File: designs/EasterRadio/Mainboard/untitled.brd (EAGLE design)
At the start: 236 x 57.5 mm, 51 parts, among them IC1 74HC595D, IC2 74HC595D, IC3 74HC595D, IC4 Analog Digital

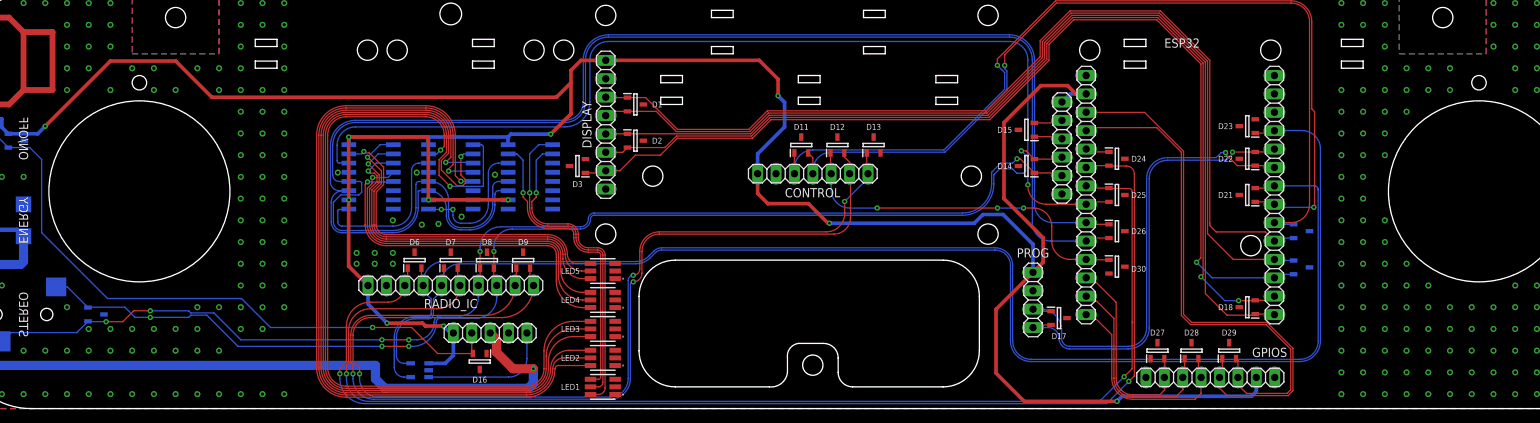
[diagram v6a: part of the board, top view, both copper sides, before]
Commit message: changes for new design excluding swap for amplifier
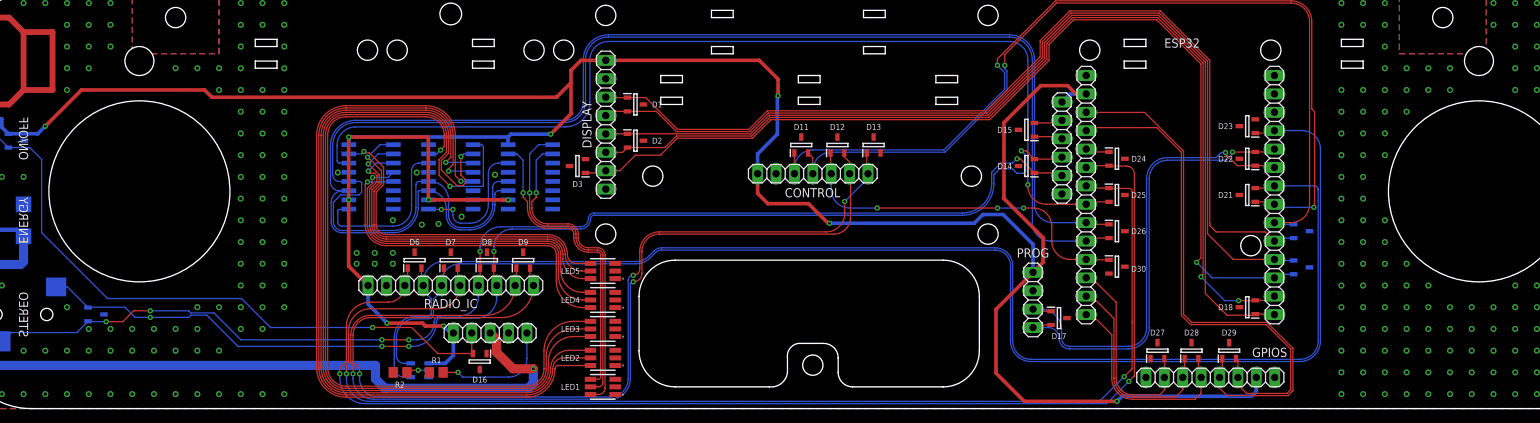
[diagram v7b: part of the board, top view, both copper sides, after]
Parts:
- added R1: 3.3K, rcl:R0805
- added R2: 10K, rcl:R0805
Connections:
- new net N$22: IC4.2, R2.1
- net GND: now also IC4.3, R1.1, R2.2; no longer IC4.2
- net U_DRAIN: now also R1.2; no longer IC4.3
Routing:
- net 3.3V: track 396.9 -> 392.8 mm
- net N$22: track 0.00 -> 3.20 mm, vias 0 -> 1
- net U_DRAIN: track 18.2 -> 16.4 mm, vias 0 -> 1
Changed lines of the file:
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@@
 <drawing>
 <settings>
-<setting alwaysvectorfont="no"/>
+<setting alwaysvectorfont="yes"/>
 <setting verticaltext="up"/>
 </settings>
@@
 <wire x1="120" y1="49" x2="120" y2="50" width="0" layer="20"/>
 <hole x="63" y="54.5" drill="3"/>
-<hole x="20" y="45" drill="2"/>
-<hole x="205" y="45" drill="2"/>
+<hole x="20" y="48" drill="4"/>
+<hole x="205" y="48" drill="4"/>
 <wire x1="36" y1="51" x2="39" y2="51" width="0" layer="20"/>
 <wire x1="39" y1="51" x2="39" y2="50" width="0" layer="20"/>
@@
 <attribute name="NAME" x="158" y="19.3" size="0.8128" layer="25" align="center"/>
 </element>
+<element name="R1" library="rcl" library_urn="urn:adsk.eagle:library:334" package="R0805" package3d_urn="urn:adsk.eagle:package:23553/2" value="3.3K" x="61" y="5" smashed="yes">
+<attribute name="NAME" x="60.365" y="6.27" size="0.8128" layer="25"/>
+<attribute name="POPULARITY" value="86" x="61" y="5" size="1.778" layer="27" display="off"/>
+<attribute name="SPICEPREFIX" value="R" x="61" y="5" size="1.778" layer="27" display="off"/>
+</element>
+<element name="R2" library="rcl" library_urn="urn:adsk.eagle:library:334" package="R0805" package3d_urn="urn:adsk.eagle:package:23553/2" value="10K" x="56" y="5" smashed="yes" rot="R180">
+<attribute name="NAME" x="56.635" y="3.73" size="0.8128" layer="25" rot="R180"/>
+<attribute name="POPULARITY" value="86" x="56" y="5" size="1.778" layer="27" rot="R180" display="off"/>
+<attribute name="SPICEPREFIX" value="R" x="56" y="5" size="1.778" layer="27" rot="R180" display="off"/>
+</element>
 </elements>
 <signals>
@@
 <contactref element="PROG" pad="3"/>
 <contactref element="ESP32" pad="14"/>
-<contactref element="IC4" pad="2"/>
 <contactref element="POWER" pad="2"/>
 <contactref element="D4" pad="2"/>
@@
 <via x="201" y="47" extent="1-16" drill="0.45"/>
 <via x="207" y="53" extent="1-16" drill="0.45"/>
-<via x="207" y="50" extent="1-16" drill="0.45"/>
 <via x="201" y="44" extent="1-16" drill="0.45"/>
 <via x="195" y="20" extent="1-16" drill="0.45"/>
@@
 <via x="37" y="53" extent="1-16" drill="0.45"/>
 <via x="37" y="44" extent="1-16" drill="0.45"/>
-<via x="22" y="47" extent="1-16" drill="0.45"/>
-<via x="22" y="44" extent="1-16" drill="0.45"/>
-<via x="25" y="44" extent="1-16" drill="0.45"/>
-<via x="19" y="47" extent="1-16" drill="0.45"/>
+<via x="25" y="47" extent="1-16" drill="0.45"/>
 <via x="16" y="56" extent="1-16" drill="0.45"/>
 <via x="16" y="53" extent="1-16" drill="0.45"/>
 <via x="16" y="50" extent="1-16" drill="0.45"/>
-<via x="16" y="44" extent="1-16" drill="0.45"/>
 <via x="10" y="56" extent="1-16" drill="0.45"/>
 <via x="10" y="53" extent="1-16" drill="0.45"/>
@@
 <contactref element="GPIOS" pad="1"/>
 <contactref element="D30" pad="3"/>
+<contactref element="IC4" pad="3"/>
+<contactref element="R1" pad="1"/>
+<contactref element="R2" pad="2"/>
 </signal>
 <signal name="N$1">
@@
 <wire x1="108.2" y1="45.5" x2="108.2" y2="43.2" width="0.508" layer="1"/>
 <via x="108.2" y="43.2" extent="1-16" drill="0.35"/>
-<wire x1="108.2" y1="43.2" x2="109.1" y2="42.3" width="0.508" layer="16"/>
 <wire x1="115.3" y1="25.6" x2="115.1" y2="25.6" width="0.508" layer="1"/>
 <via x="115.3" y="25.6" extent="1-16" drill="0.35"/>
@@
 <wire x1="5.95" y1="37.95" x2="1.9" y2="37.95" width="0.508" layer="16"/>
 <wire x1="77.6" y1="43" x2="30" y2="43" width="0.508" layer="1"/>
-<wire x1="30" y1="43" x2="25" y2="48" width="0.508" layer="1"/>
-<wire x1="25" y1="48" x2="16" y2="48" width="0.508" layer="1"/>
-<wire x1="16" y1="48" x2="7" y2="39" width="0.508" layer="1"/>
+<wire x1="30" y1="43" x2="29" y2="44" width="0.508" layer="1"/>
+<wire x1="29" y1="44" x2="12" y2="44" width="0.508" layer="1"/>
+<wire x1="12" y1="44" x2="7" y2="39" width="0.508" layer="1"/>
 <wire x1="1.9" y1="37.95" x2="1" y2="38.85" width="0.508" layer="16"/>
 <wire x1="1" y1="38.85" x2="1" y2="40" width="0.508" layer="16"/>
@@
 <contactref element="CONTROL" pad="7"/>
 <wire x1="105.38" y1="35.18" x2="105.38" y2="32.44" width="0.508" layer="16"/>
-<wire x1="109.1" y1="42.3" x2="109.1" y2="38.9" width="0.508" layer="16"/>
-<wire x1="109.1" y1="38.9" x2="105.38" y2="35.18" width="0.508" layer="16"/>
+<wire x1="108.2" y1="43.2" x2="108.1" y2="43.1" width="0.508" layer="16"/>
+<wire x1="108.1" y1="43.1" x2="108.1" y2="37.9" width="0.508" layer="16"/>
+<wire x1="108.1" y1="37.9" x2="105.38" y2="35.18" width="0.508" layer="16"/>
 <wire x1="105.38" y1="29.72" x2="105.38" y2="32.44" width="0.508" layer="1"/>
 <wire x1="115.1" y1="25.6" x2="112.4" y2="28.3" width="0.508" layer="1"/>
@@
 </signal>
 <signal name="U_DRAIN">
-<contactref element="IC4" pad="3"/>
 <contactref element="POWER" pad="1"/>
-<wire x1="59.95" y1="4.35" x2="70.98" y2="4.35" width="0.1524" layer="16"/>
-<wire x1="70.98" y1="4.35" x2="73.52" y2="6.89" width="0.1524" layer="16" curve="90"/>
+<wire x1="73.52" y1="6.89" x2="70.98" y2="4.35" width="0.1524" layer="16" curve="-90"/>
 <wire x1="73.52" y1="6.89" x2="73.52" y2="10.44" width="0.1524" layer="16"/>
+<contactref element="R1" pad="2"/>
+<wire x1="70.98" y1="4.35" x2="64.65" y2="4.35" width="0.1524" layer="16"/>
+<wire x1="64.65" y1="4.35" x2="64" y2="5" width="0.1524" layer="16"/>
+<via x="64" y="5" extent="1-16" drill="0.35"/>
+<wire x1="64" y1="5" x2="61.95" y2="5" width="0.1524" layer="1"/>
 </signal>
 <signal name="5V">
@@
 <wire x1="146" y1="23.14" x2="146" y2="25.16" width="0.1524" layer="1"/>
 </signal>
+<signal name="N$22">
+<contactref element="R2" pad="1"/>
+<contactref element="IC4" pad="2"/>
+<via x="58.5" y="5.3" extent="1-16" drill="0.35"/>
+<wire x1="56.95" y1="5" x2="57.25" y2="5" width="0.1524" layer="1"/>
+<wire x1="57.5105375" y1="5.2605375" x2="57.25" y2="5" width="0.1524" layer="1"/>
+<wire x1="57.5105375" y1="5.2605375" x2="57.473378125" y2="5.3" width="0.1524" layer="1"/>
+<wire x1="57.473378125" y1="5.3" x2="58.5" y2="5.3" width="0.1524" layer="1"/>
+<wire x1="58.5" y1="5.3" x2="59.95" y2="5.3" width="0.1524" layer="16"/>
+</signal>
 </signals>

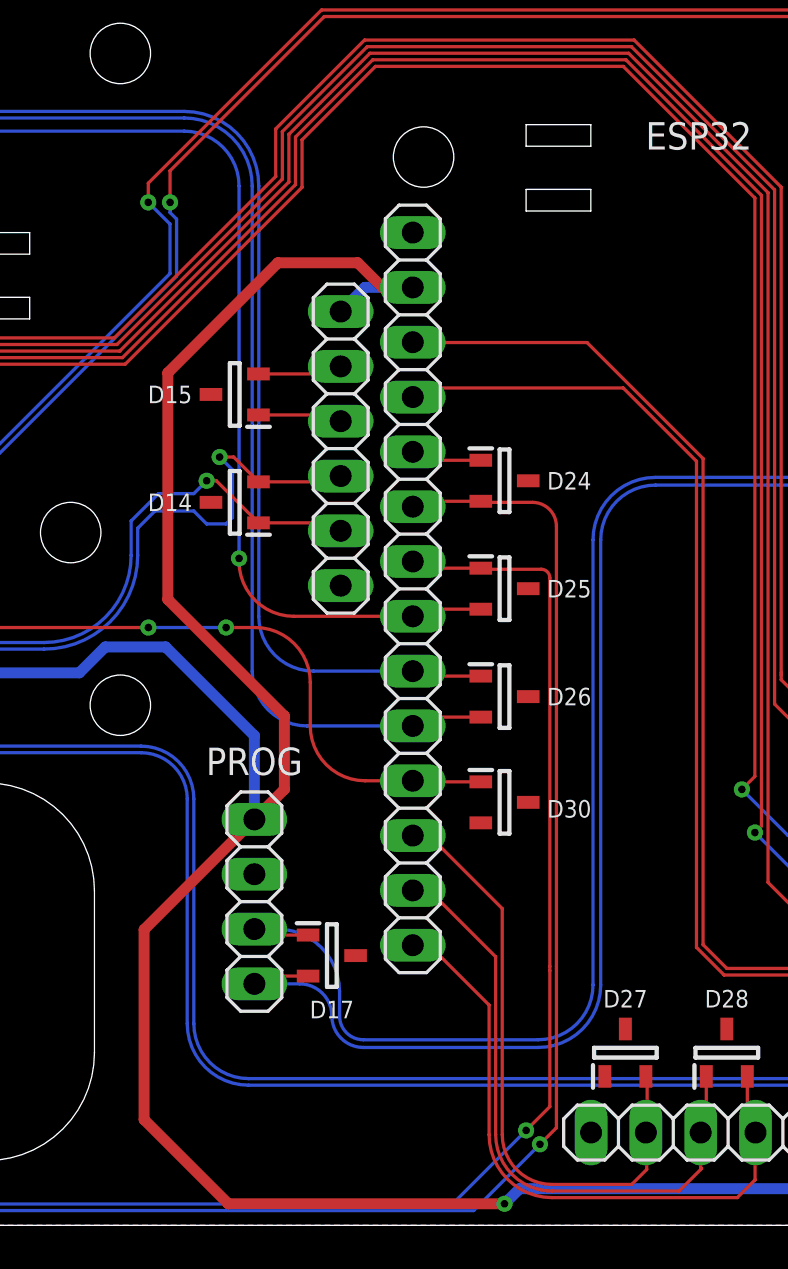
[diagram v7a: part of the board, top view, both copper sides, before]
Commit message: changes for new design including swap for amplifier
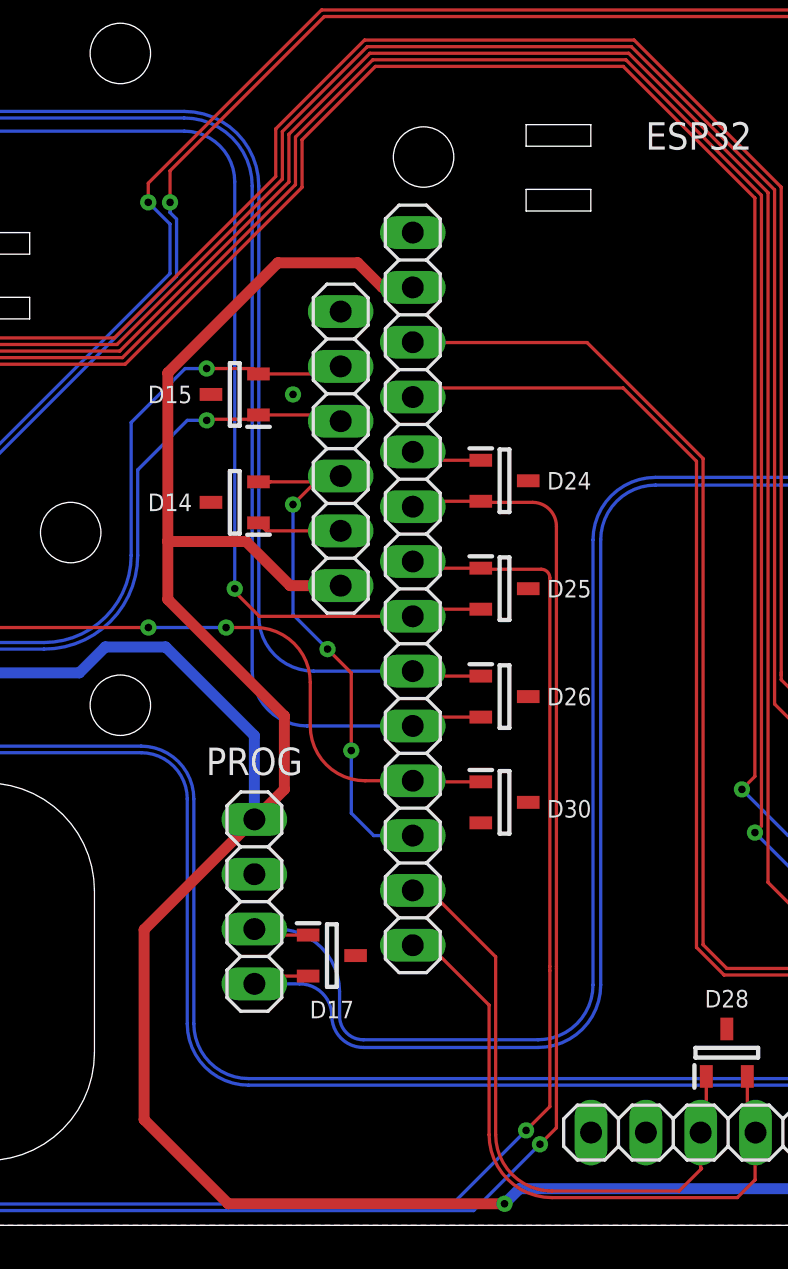
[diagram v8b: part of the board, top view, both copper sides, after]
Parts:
- removed D27: PESD3V3L2BT,215, MouserUseful:SOT95P230X110-3N
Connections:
- removed net IO14: D27.2, ESP32.3, GPIOS.2
- net !MUTE: now also AMPLIFIER.5, D14.1; no longer AMPLIFIER.2, D15.2
- net !SHDN: now also AMPLIFIER.4, D14.2, ESP32.3; no longer AMPLIFIER.3, D15.1
- net 3.3V: now also AMPLIFIER.6; no longer AMPLIFIER.1
- net GND: now also AMPLIFIER.1, GPIOS.2; no longer AMPLIFIER.6, D27.3
- net INL: now also AMPLIFIER.3, D15.1; no longer AMPLIFIER.4, D14.2
- net INR: now also AMPLIFIER.2, D15.2; no longer AMPLIFIER.5, D14.1
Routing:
- net IO14: track 28.3 -> 0.00 mm
- net !SHDN: track 3.93 -> 24.7 mm, vias 0 -> 3
- net 3.3V: track 392.8 -> 397.9 mm
- net INR: track 165.9 -> 170.0 mm
- net INL: track 162.7 -> 161.7 mm
- net DS: track 139.5 -> 140.4 mm
